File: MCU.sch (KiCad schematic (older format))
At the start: 9 parts, among them J2 STLinkV2, SW1 SW_SPST, U13 STM32F051K4Tx

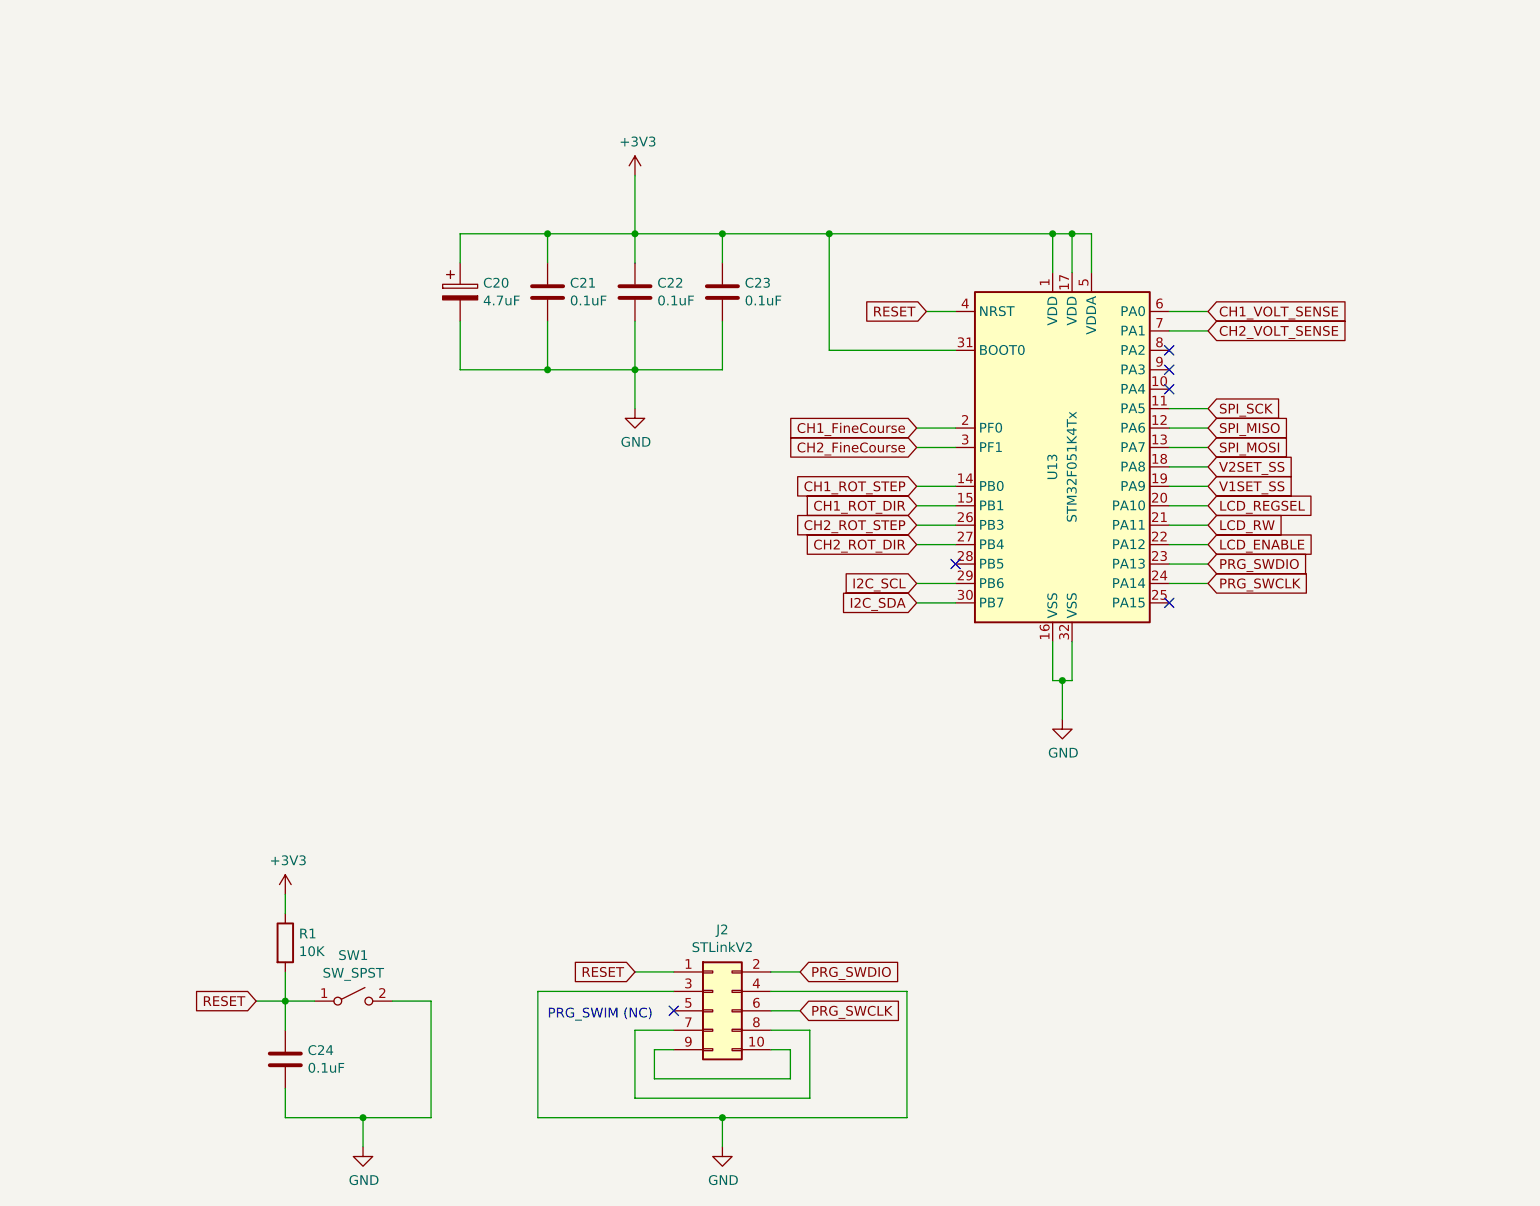
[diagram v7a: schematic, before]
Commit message: Replaced digital pots with analog, removed spi bus too as no longer needed
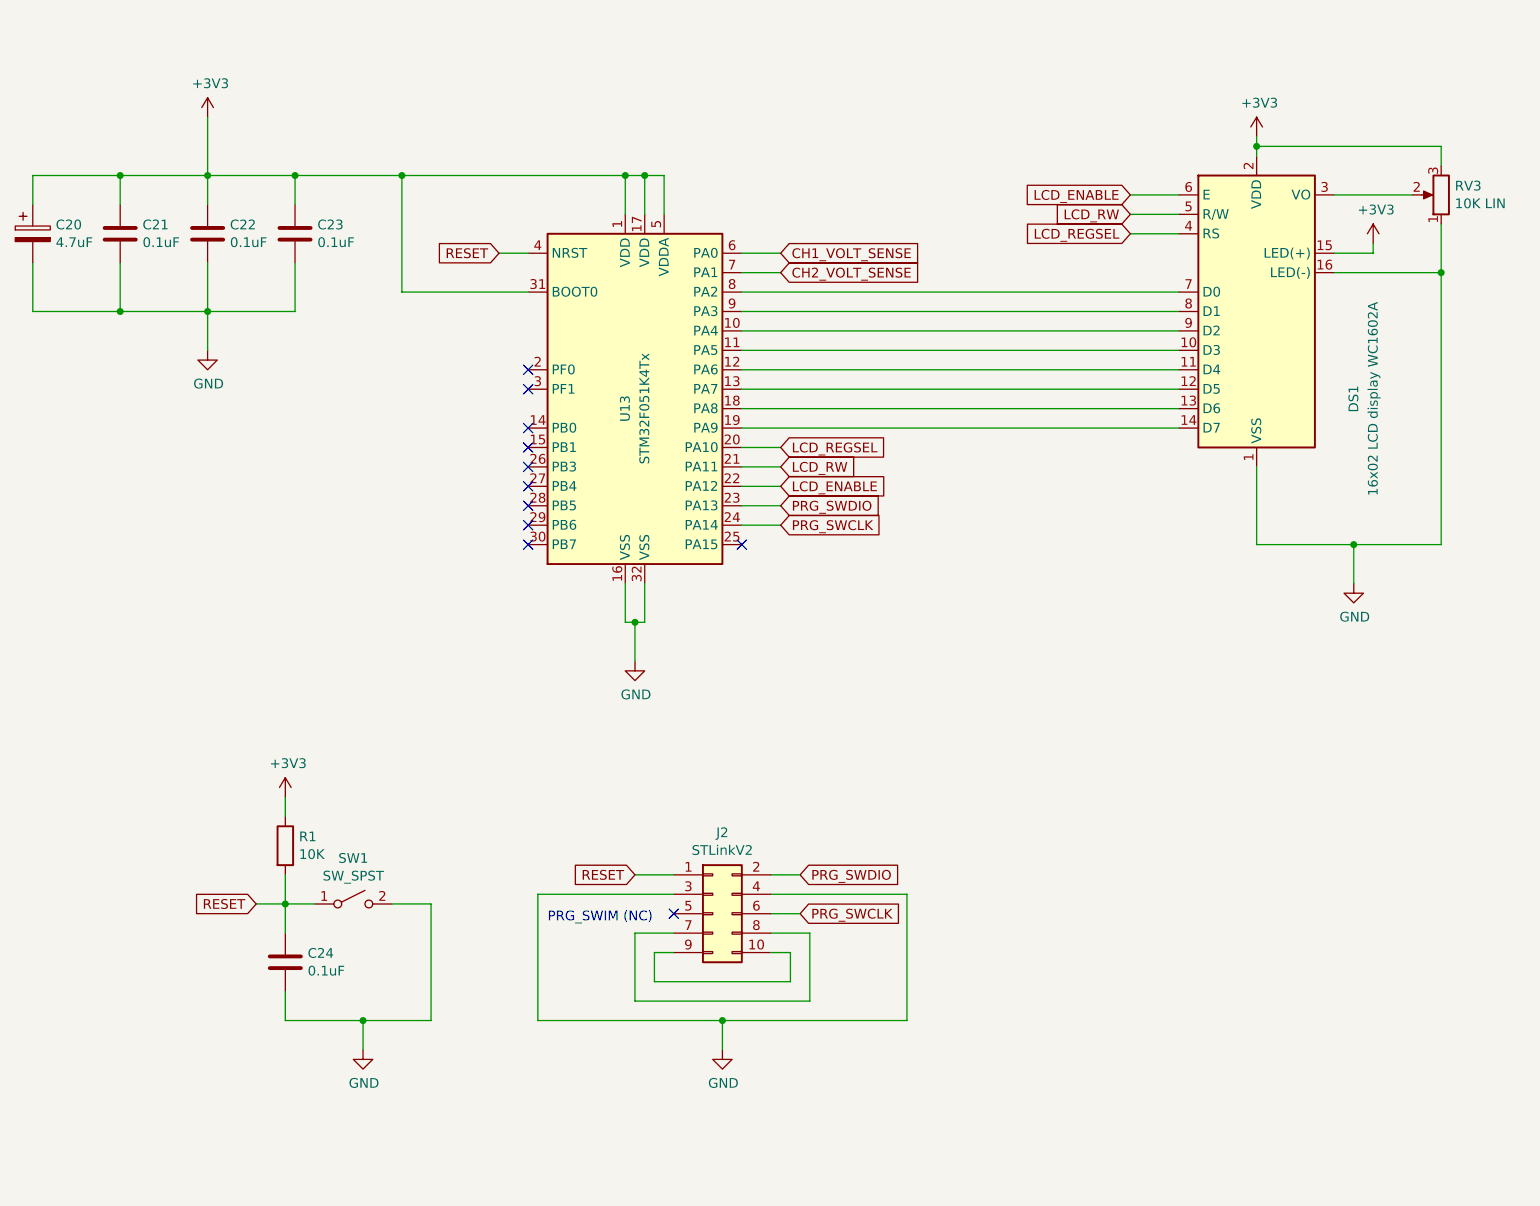
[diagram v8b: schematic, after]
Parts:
- added DS1: 16x02 LCD display WC1602A, Display:WC1602A, symbol Display_Character:WC1602A
- added RV3: 10K LIN, symbol Device:R_POT
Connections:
- net +3V3: now also DS1.15 (LED(+)), DS1.2 (VDD), RV3.3
- net GND: now also DS1.1 (VSS), DS1.16 (LED(-)), RV3.1
- net LCD_ENABLE: now also DS1.6 (E)
- net LCD_REGSEL: now also DS1.4 (RS)
- net LCD_RW: now also DS1.5 (R/W)
- net at U13.10 (PA4): now also DS1.9 (D2)
- net at U13.8 (PA2): now also DS1.7 (D0)
- net at U13.9 (PA3): now also DS1.8 (D1)
- net CH1_FineCourse: no longer names the net of U13.2 (PF0)
- net CH1_ROT_DIR: no longer names the net of U13.15 (PB1)
- net CH1_ROT_STEP: no longer names the net of U13.14 (PB0)
- net CH2_FineCourse: no longer names the net of U13.3 (PF1)
- net CH2_ROT_DIR: no longer names the net of U13.27 (PB4)
- net CH2_ROT_STEP: no longer names the net of U13.26 (PB3)
- net I2C_SCL: no longer names the net of U13.29 (PB6)
- net I2C_SDA: no longer names the net of U13.30 (PB7)
- net SPI_MISO: no longer names the net of U13.12 (PA6)
- net SPI_MISO: now also DS1.11 (D4)
- net SPI_MOSI: no longer names the net of U13.13 (PA7)
- net SPI_MOSI: now also DS1.12 (D5)
- net SPI_SCK: no longer names the net of U13.11 (PA5)
- net SPI_SCK: now also DS1.10 (D3)
- net V1SET_SS: no longer names the net of U13.19 (PA9)
- net V1SET_SS: now also DS1.14 (D7)
- net V2SET_SS: no longer names the net of U13.18 (PA8)
- net V2SET_SS: now also DS1.13 (D6)
- new net: DS1.3 (VO), RV3.2
- no-connect marks 6 -> 11
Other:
- moved on the sheet: C20, C21, C22, C23, C24, J2, R1, SW1, U13
